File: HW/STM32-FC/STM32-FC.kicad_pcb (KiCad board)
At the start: 4 copper layers, 39 x 48.5 mm, 114 parts, among them J1 GH 1.25mm 6P, J10 GH 1.25mm 6P, J11 GH 1.25mm 6P, J12 GH 1.25mm 6P, J13 GH 1.25mm 4P, J14 GH 1.25mm 4P, J15 GH 1.25mm 4P, J2 USB_C_USB2.0_14P, J3 GH 1.25mm 6P, J4 Micro_SD_Card_Det1, J5 JST ZH 1.5mm 2P, J6 PWM_Conn_3x14, J7 ZH 1.5mm 3P, J8 ZH 1.5mm 4P, J9 GH 1.25mm 10P, Q1 S9013, Q2 S9013, SW2 SW_DIP_x03, U1 STM32F407VETx, U10 ATA6561-GBQW, U11 ATA6561-GBQW, U2 USBLC6-2SC6, U3 AMS1117-3.3, U4 AMS1117-3.3, U5 W25X40CLUXIG, U6 BMI323, U7 ICM-42688-P, U8 LIS2MDLTR, U9 LPS22HH, Y1 16MHz

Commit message: 2025.02.11 PCB DONE! MEMO UPDATING
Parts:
- J2: footprint USB_C:918-418K2023S40023 -> Connector_USB:USB_C_Receptacle_GCT_USB4110
- J4: value Micro_SD_Card_Det1 -> TF-06A; footprint Connector_Card:microSD_HC_Hirose_DM3D-SF -> TF-06A:TF06A
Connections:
- R15 pad 2: Net-(J4-DET) -> Net-(J4-SWICTH)
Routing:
- net /SPI2_MISO: track 51.0 -> 35.1 mm
- net /SPI2_SCK: track 47.2 -> 35.1 mm
- net /MSD_DETECT: track 28.3 -> 21.3 mm
- net /CAN2_TX: track 17.8 -> 12.6 mm
- net Net-(J4-DET): track 4.43 -> 0.00 mm, vias 1 -> 0
- net Net-(J4-SWICTH): track 0.00 -> 4.05 mm, vias 0 -> 1
- net /MSD_NSS: track 17.4 -> 20.5 mm, vias 3 -> 2
- net GND: track 171.6 -> 169.1 mm, vias 40 -> 41
- net +3.3V: track 129.0 -> 130.5 mm, vias 25 -> 24
- net /FLASH_NSS: track 22.5 -> 23.8 mm
- net /CAN2_RX: track 21.6 -> 20.4 mm
- net /SPI2_MOSI: track 39.9 -> 38.8 mm, vias 3 -> 2
- net /SPI1_MOSI: track 23.4 -> 22.9 mm
- net /SPI1_MISO: track 24.2 -> 23.7 mm

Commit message: Test software v1
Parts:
- added R10: 5k1, Resistor_SMD:R_0402_1005Metric, F.Cu at (128.6, 88.2)
- added REF**: MountingHole_2.2mm_M2_DIN965_Pad, MountingHole:MountingHole_2.2mm_M2_DIN965_Pad, F.Cu at (200.5, 100.5)
- added REF**: MountingHole_2.2mm_M2_DIN965_Pad, MountingHole:MountingHole_2.2mm_M2_DIN965_Pad, F.Cu at (200.5, 70.0)
- added REF**: MountingHole_2.2mm_M2_DIN965_Pad, MountingHole:MountingHole_2.2mm_M2_DIN965_Pad, F.Cu at (170.0, 100.5)
- added REF**: MountingHole_2.2mm_M2_DIN965_Pad, MountingHole:MountingHole_2.2mm_M2_DIN965_Pad, F.Cu at (170.0, 70.0)
- moved R9 5.20 mm to (128.5, 83.0), turned to 90 degrees
- moved J4 1.25 mm to (150.0, 87.0), turned to 90 degrees
- renumbered C9 to C10, C10 to C11, C11 to C12, C12 to C13, C13 to C14, C14 to C15, C15 to C16, C16 to C17, C17 to C18, C18 to C19, C19 to C20, C20 to C21, C21 to C22, C22 to C23, C23 to C24, C24 to C25, C25 to C26, C26 to C27, C27 to C28, C28 to C29, C29 to C30, C30 to C31, C31 to C32, C32 to C33, C33 to C34, C34 to C35, C35 to C5, C5 to C6, C6 to C7, C7 to C8, C8 to C9, J8 to J7, J7 to J8, R3 to R1, R10 to R11, R11 to R12, R12 to R13, R13 to R14, R14 to R15, R15 to R16, R16 to R17, R17 to R18, R18 to R19, R1 to R2, R19 to R20, R20 to R21, R21 to R22, R22 to R23, R23 to R24, R24 to R25, R25 to R26, R26 to R27, R27 to R28, R28 to R29, R2 to R3, R29 to R30, R30 to R31, R31 to R32, R32 to R33, R33 to R34, R34 to R35, SW2 to SW1
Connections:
- net /TIM1_CH4 renamed /PPM_IN
- net /UART1_RX renamed /DSM/SBUS
- net /UART1_TX renamed /SRXL2
- J2 pad B5: Net-(J2-CC1) -> Net-(J2-CC2)
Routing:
- net /SPI2_MISO: track 35.1 -> 45.1 mm
- net /MSD_NSS: track 20.5 -> 13.5 mm
- net /DSM/SBUS: track 119.1 -> 112.4 mm
- net GND: track 169.1 -> 162.8 mm
- net Net-(J4-SWICTH): track 4.05 -> 8.76 mm
- net /SPI2_MOSI: track 38.8 -> 43.4 mm
- net /SPI2_SCK: track 35.1 -> 39.7 mm
- net Net-(J2-CC1): track 6.58 -> 2.06 mm
- net +3.3V: track 130.5 -> 127.9 mm, vias 24 -> 25
- net Net-(J2-CC2): track 0.00 -> 1.77 mm
- net /PPM_IN: track 52.9 -> 54.6 mm
- net +5V: track 53.2 -> 54.6 mm
- net /UART5_TX: track 62.3 -> 61.0 mm
- net /CAN2_RX: track 20.4 -> 21.7 mm
- net /UART2_RTS: track 27.6 -> 28.3 mm

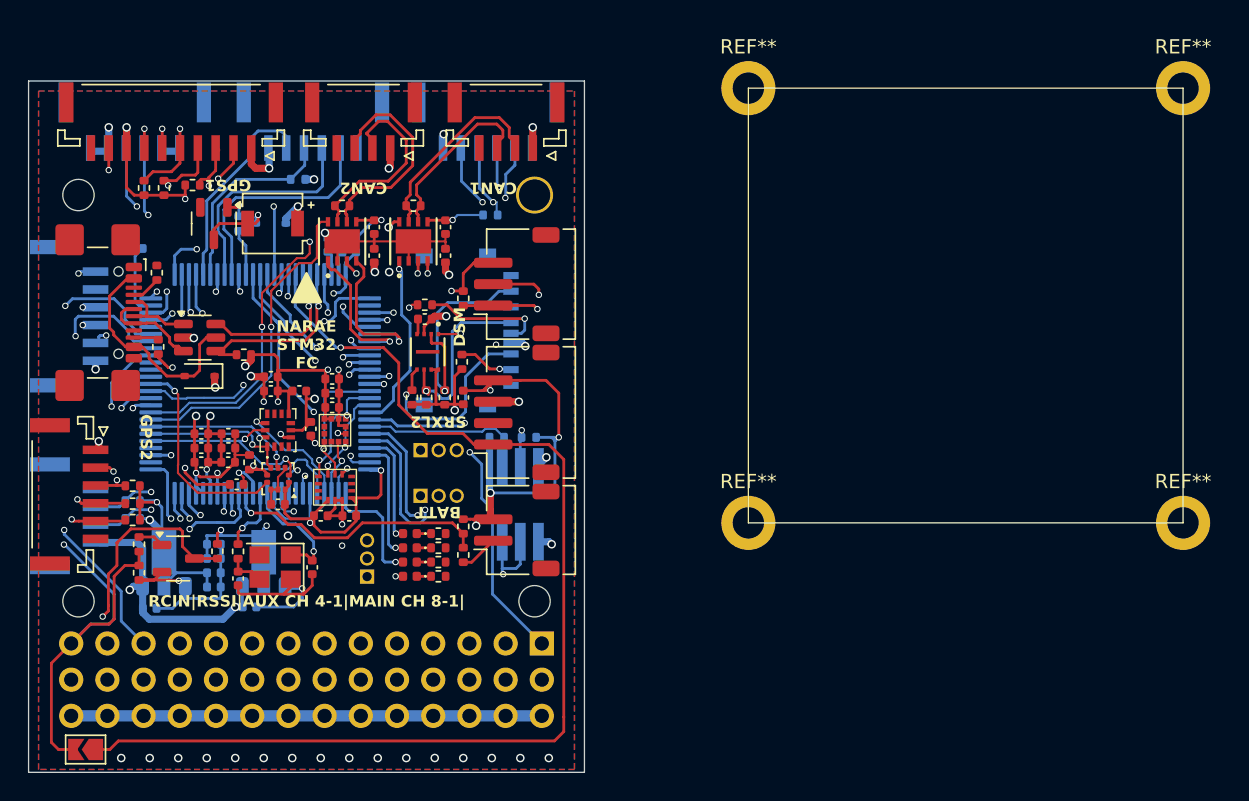
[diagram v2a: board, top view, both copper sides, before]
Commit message: SRXL2_readByte() array index out bug fix
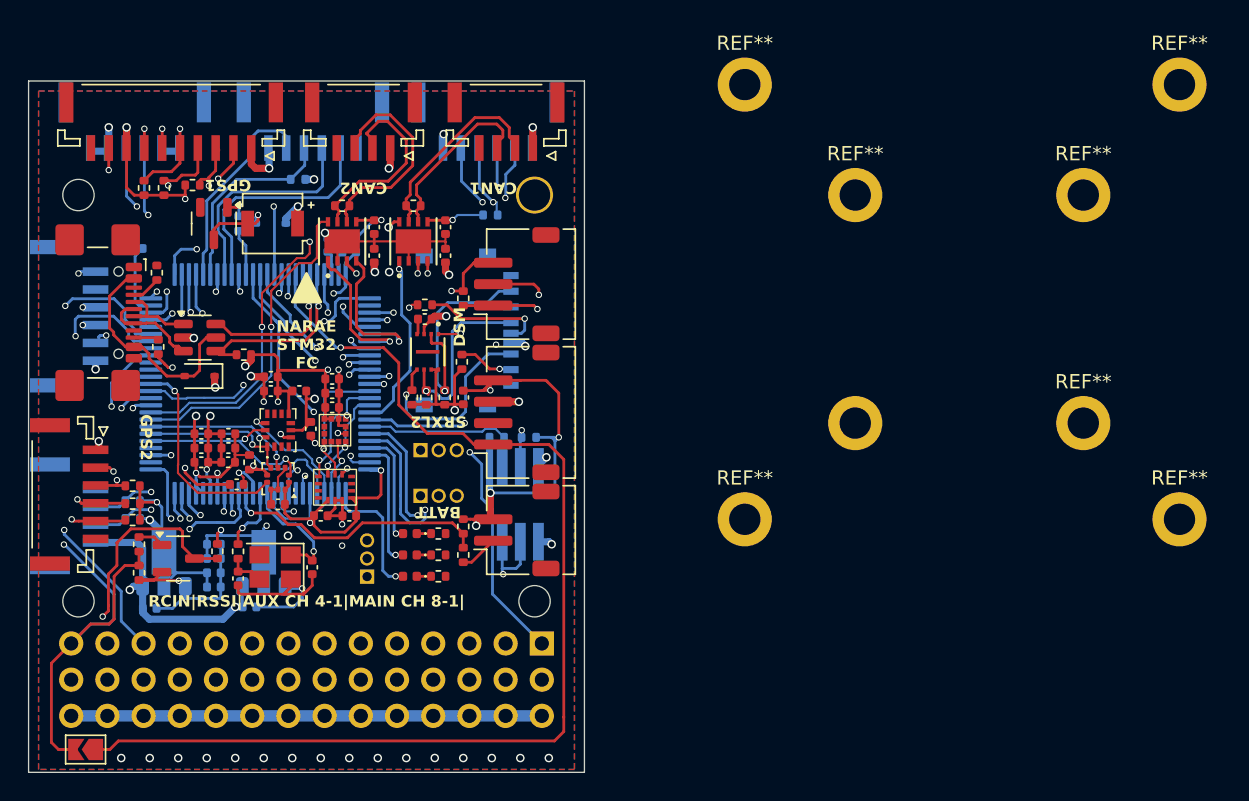
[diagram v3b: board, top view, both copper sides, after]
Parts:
- removed D1: White, LED_SMD:LED_0402_1005Metric
- removed R4: 1k, Resistor_SMD:R_0402_1005Metric
- added ?: , , F.Cu at (177.5, 93.5)
- added REF**: MountingHole_2.2mm_M2_DIN965_Pad, MountingHole:MountingHole_2.2mm_M2_DIN965_Pad, F.Cu at (193.5, 93.5)
- added REF**: MountingHole_2.2mm_M2_DIN965_Pad, MountingHole:MountingHole_2.2mm_M2_DIN965_Pad, F.Cu at (177.5, 77.5)
- added REF**: MountingHole_2.2mm_M2_DIN965_Pad, MountingHole:MountingHole_2.2mm_M2_DIN965_Pad, F.Cu at (193.5, 77.5)
- R6, R7, R8: value 1k -> 220
- moved D5 1.00 mm to (146.2, 104.2)
- moved R8 1.00 mm to (148.2, 104.2)
- moved D4 0.50 mm to (146.2, 102.8)
- moved R7 0.50 mm to (148.2, 102.8)
- moved REF** 0.35 mm to (200.2, 100.2)
- moved REF** 0.35 mm to (200.2, 69.8)
- moved REF** 0.35 mm to (169.8, 100.2)
- moved REF** 0.35 mm to (169.8, 69.8)
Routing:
- net Net-(D1-K): track 1.00 -> 0.00 mm
- net /LED_BLUE: track 7.83 -> 8.68 mm
- net +3.3V: track 127.9 -> 127.4 mm, vias 25 -> 24
- net /LED_YELLOW: track 8.06 -> 8.56 mm

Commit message: Log add. backup
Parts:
- removed JP1: SolderJumper_2_Open, Jumper:SolderJumper-2_P1.3mm_Open_TrianglePad1.0x1.5mm
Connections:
- U6 pad 4: unconnected-(U6-INT1-Pad4) -> /GYRO2_INT
- U7 pad 9: unconnected-(U7-INT2/FSYNC/CLKIN-Pad9) -> /GYRO1_INT
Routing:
- net /SRXL2: track 79.7 -> 21.9 mm
- net /DSM/SBUS: track 112.4 -> 81.9 mm
- net /PPM_IN: track 54.6 -> 45.2 mm
